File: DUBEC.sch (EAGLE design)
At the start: 46 parts

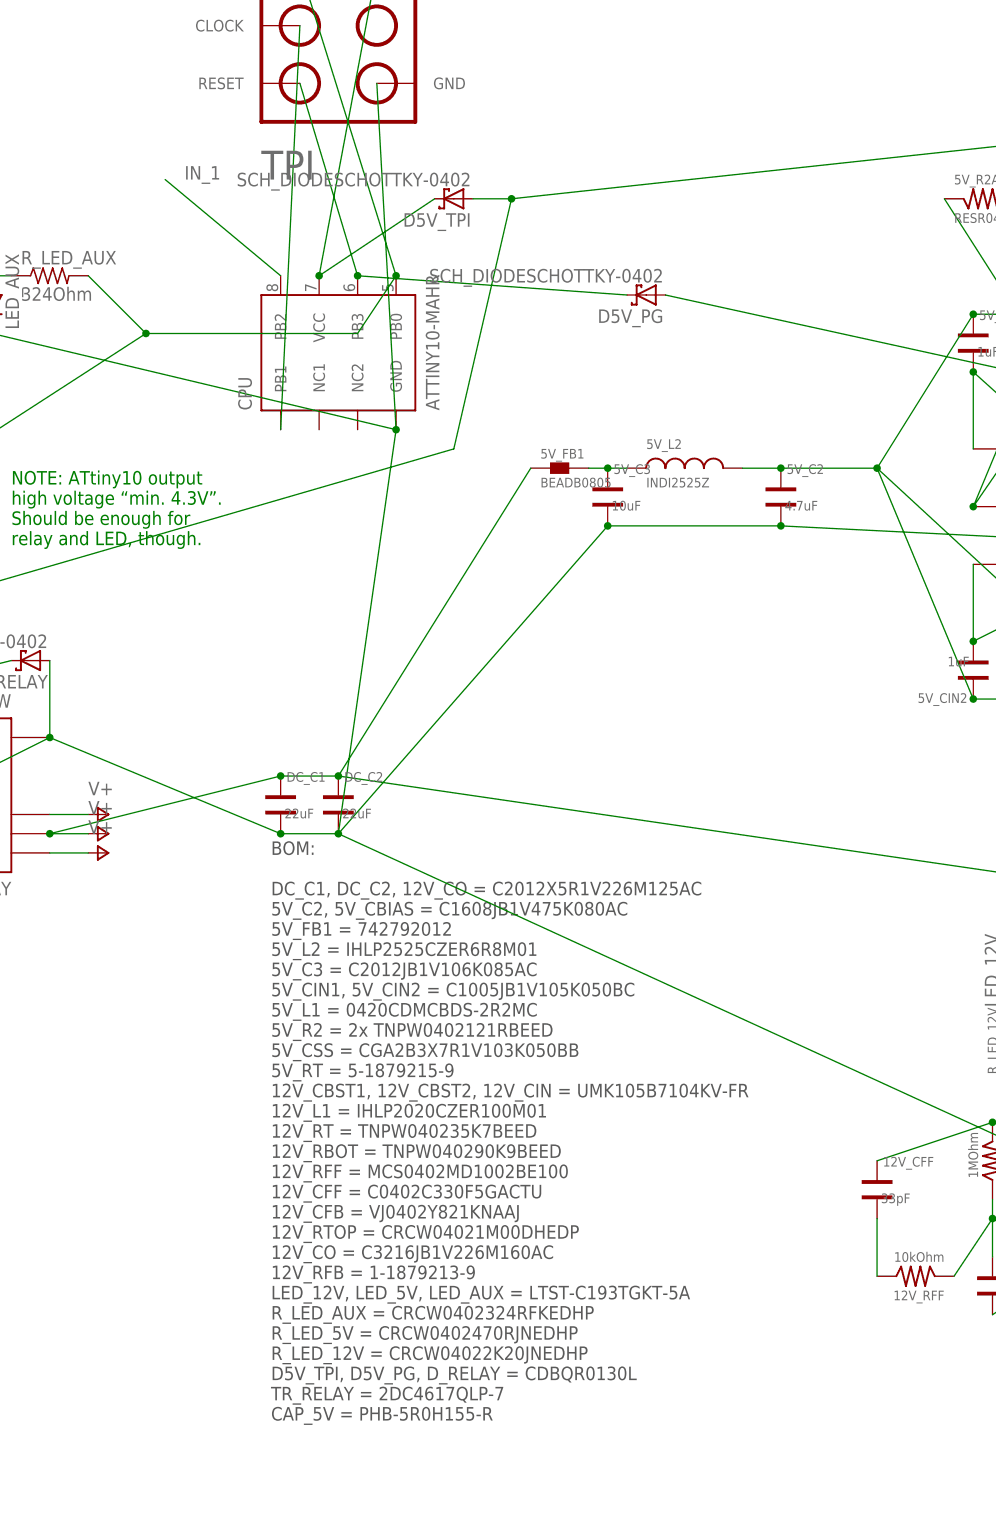
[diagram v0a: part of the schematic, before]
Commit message: Preci-Dip TPI socket
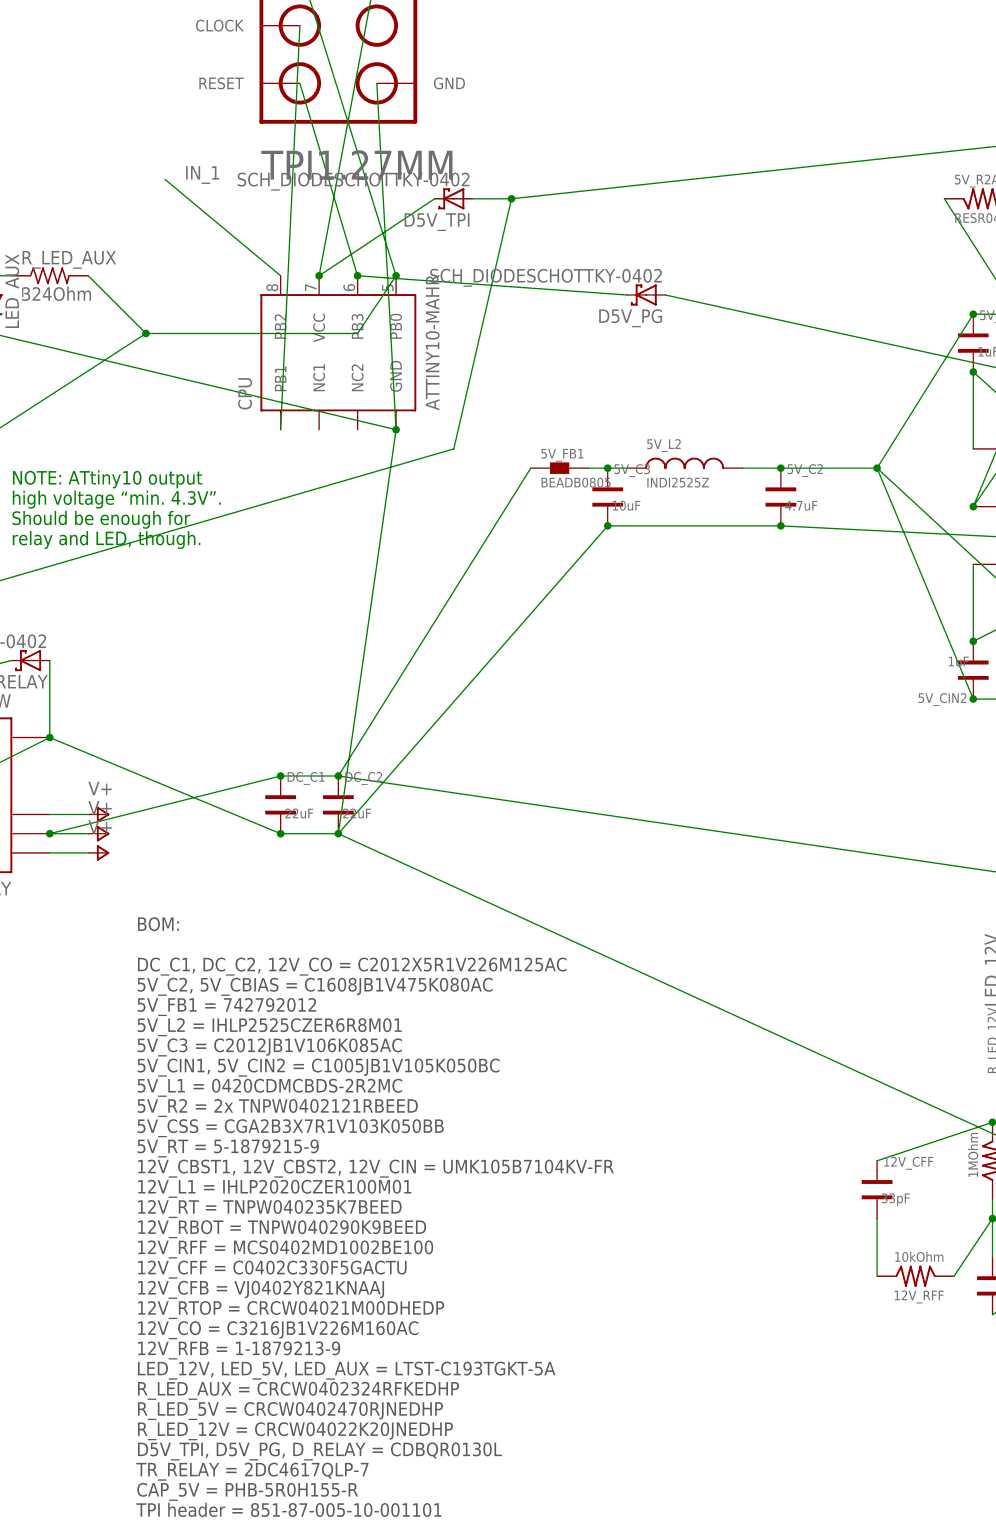
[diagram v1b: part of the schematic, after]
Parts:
- U$1: value TPI -> TPI1.27MM; device dubec:TPI -> dubec:TPI1.27MM
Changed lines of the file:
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@@
 <part name="R_LED_12V" library="jne" deviceset="RES" device="R0402" value="2.2kOhm"/>
 <part name="R_LED_5V" library="jne" deviceset="RES" device="R0402" value="470Ohm"/>
-<part name="U$1" library="dubec" deviceset="TPI" device=""/>
+<part name="U$1" library="dubec" deviceset="TPI" device="1.27MM" value="TPI1.27MM"/>
 <part name="D5V_PG" library="dubec" deviceset="SCH_DIODE" device="SCHOTTKY-0402"/>
 <part name="D5V_TPI" library="dubec" deviceset="SCH_DIODE" device="SCHOTTKY-0402"/>
@@
 <sheet>
 <plain>
-<text x="-49.53" y="-95.25" size="1.778" layer="97">BOM:
+<text x="-67.31" y="-107.95" size="1.778" layer="97">BOM:
 DC_C1, DC_C2, 12V_CO = C2012X5R1V226M125AC
 5V_C2, 5V_CBIAS = C1608JB1V475K080AC
@@
 TR_RELAY = 2DC4617QLP-7
 CAP_5V = PHB-5R0H155-R
+TPI header = 851-87-005-10-001101
 </text>
 <text x="-83.82" y="20.32" size="1.778" layer="91">NOTE: ATtiny10 output

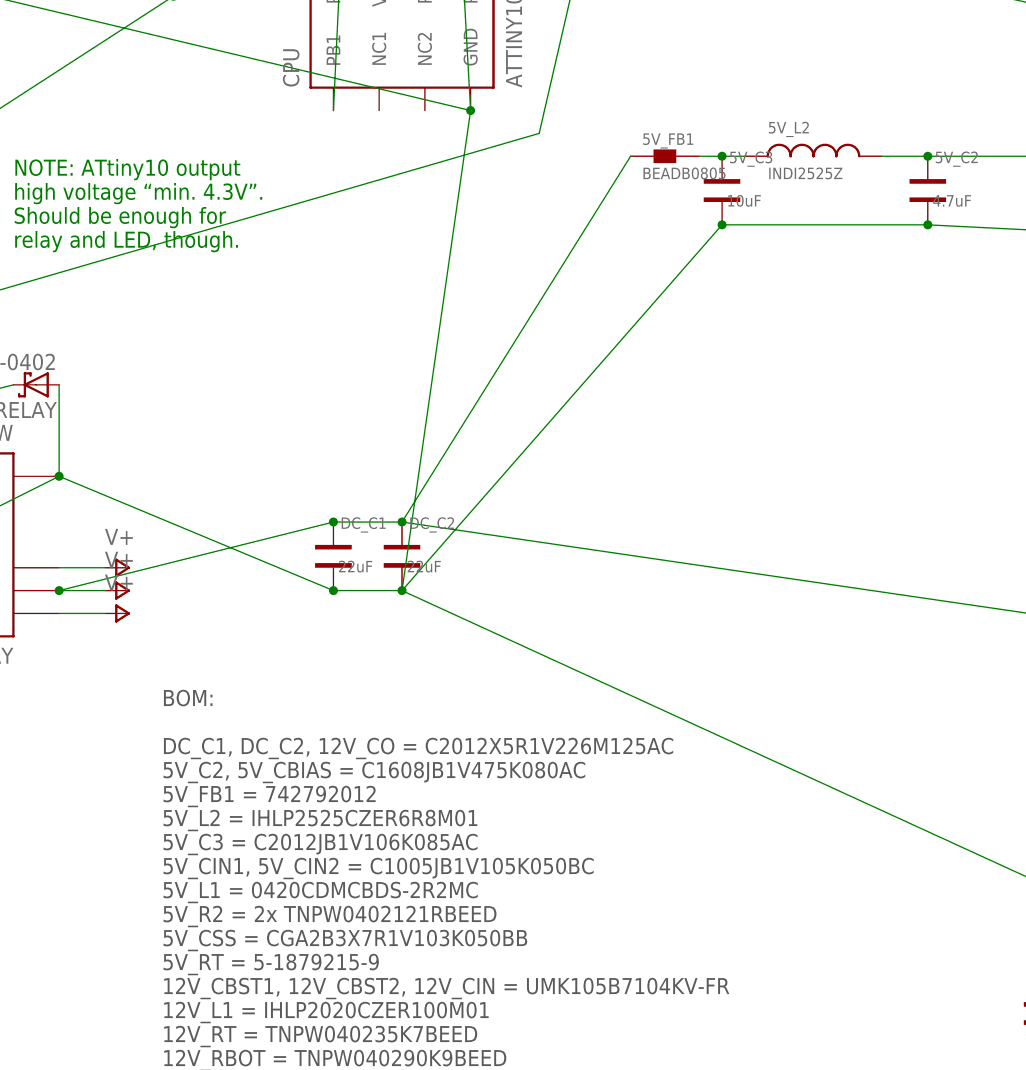
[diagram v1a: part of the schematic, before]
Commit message: Recommended inductor for 5V
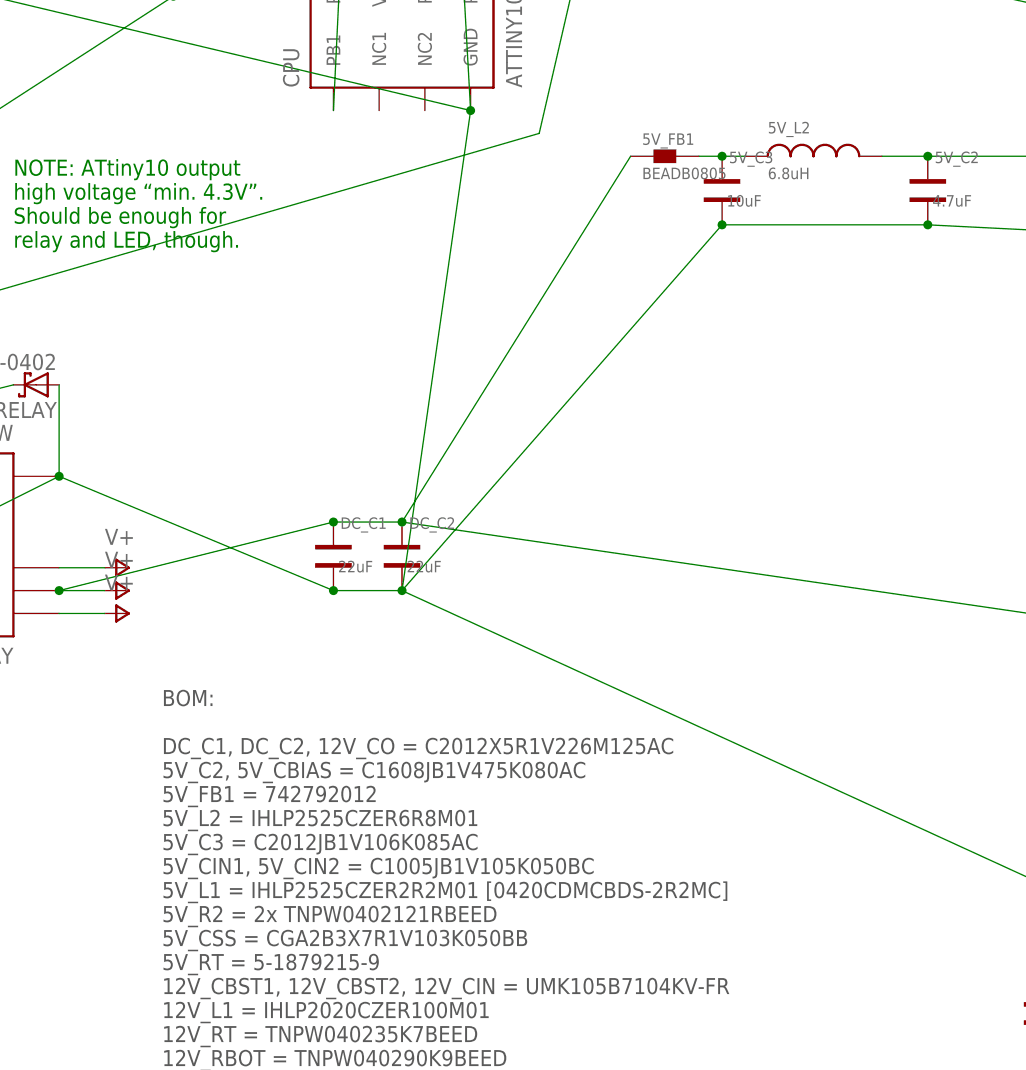
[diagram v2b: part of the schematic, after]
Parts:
- 5V_L1: device jne:INDI0420CDMCB/DS -> dubec:INDI2525Z
- 5V_L2: value INDI2525Z -> 6.8uH
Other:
- note added: "BOM: DC_C1, DC_C2, 12V_CO = C2012X5R1V226M125AC 5V_C2, 5V_CBIAS = C1608JB1V475K080AC 5V_FB1 = 742792012 5V_L2 = IHLP2525CZER6R8M01 5V_C3 = C2012JB1V106K085AC 5V_CIN1, 5V_CIN2 = C1005JB1V105K050BC 5V_L1 = IHLP2525CZER2R2M01 [0420CDMCBDS-2R2MC] 5V_R2 = 2x TNPW0402121RBEED 5V_CSS = CGA2B3X7R1V103K050BB 5V_RT = 5-1879215-9 12V_CBST1, 12V_CBST2, 12V_CIN = UMK105B7104KV-FR 12V_L1 = IHLP2020CZER100M01 1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"
- note removed: "BOM: DC_C1, DC_C2, 12V_CO = C2012X5R1V226M125AC 5V_C2, 5V_CBIAS = C1608JB1V475K080AC 5V_FB1 = 742792012 5V_L2 = IHLP2525CZER6R8M01 5V_C3 = C2012JB1V106K085AC 5V_CIN1, 5V_CIN2 = C1005JB1V105K050BC 5V_L1 = 0420CDMCBDS-2R2MC 5V_R2 = 2x TNPW0402121RBEED 5V_CSS = CGA2B3X7R1V103K050BB 5V_RT = 5-1879215-9 12V_CBST1, 12V_CBST2, 12V_CIN = UMK105B7104KV-FR 12V_L1 = IHLP2020CZER100M01 12V_RT = TNPW040235K7B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"
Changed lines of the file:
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@@
 <part name="DC_C1" library="jne" deviceset="CAP" device="C0805" value="22uF"/>
 <part name="5V_C2" library="jne" deviceset="CAP" device="C0603" value="4.7uF"/>
-<part name="5V_L2" library="jne" deviceset="IND" device="I2525Z" value="INDI2525Z"/>
+<part name="5V_L2" library="jne" deviceset="IND" device="I2525Z" value="6.8uH"/>
 <part name="5V_FB1" library="jne" deviceset="BEAD" device="B0805"/>
 <part name="5V_C3" library="jne" deviceset="CAP" device="C0805" value="10uF"/>
@@
 <part name="12V_CO" library="jne" deviceset="CAP" device="C1206" value="22uF"/>
 <part name="12V_CIN" library="jne" deviceset="CAP" device="C0402" value="0.1uF"/>
-<part name="5V_L1" library="jne" deviceset="IND" device="I0420CDMCB/DS" value="2.2uH"/>
+<part name="5V_L1" library="dubec" deviceset="IND" device="I2525Z" value="2.2uH"/>
 <part name="5V_CBST" library="jne" deviceset="CAP" device="C0402" value="0.1uF"/>
 <part name="5V_CVCC" library="jne" deviceset="CAP" device="C0402" value="1uF"/>
@@
 5V_C3 = C2012JB1V106K085AC
 5V_CIN1, 5V_CIN2 = C1005JB1V105K050BC
-5V_L1 = 0420CDMCBDS-2R2MC
+5V_L1 = IHLP2525CZER2R2M01 [0420CDMCBDS-2R2MC]
 5V_R2 = 2x TNPW0402121RBEED
 5V_CSS = CGA2B3X7R1V103K050BB

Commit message: Flyback diode
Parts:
- added D12V: SCH_DIODESCHOTTKY-0402, dubec:SCH_DIODESCHOTTKY-0402
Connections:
- net GND: now also D12V.A
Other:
- moved on the sheet: 12V_C3, 12V_CBST1, 12V_CBST2, 12V_CFB, 12V_CFF, 12V_CIN, 12V_CO, 12V_RFF, 12V_RT, 5V_C2, 5V_C3, 5V_CIN1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

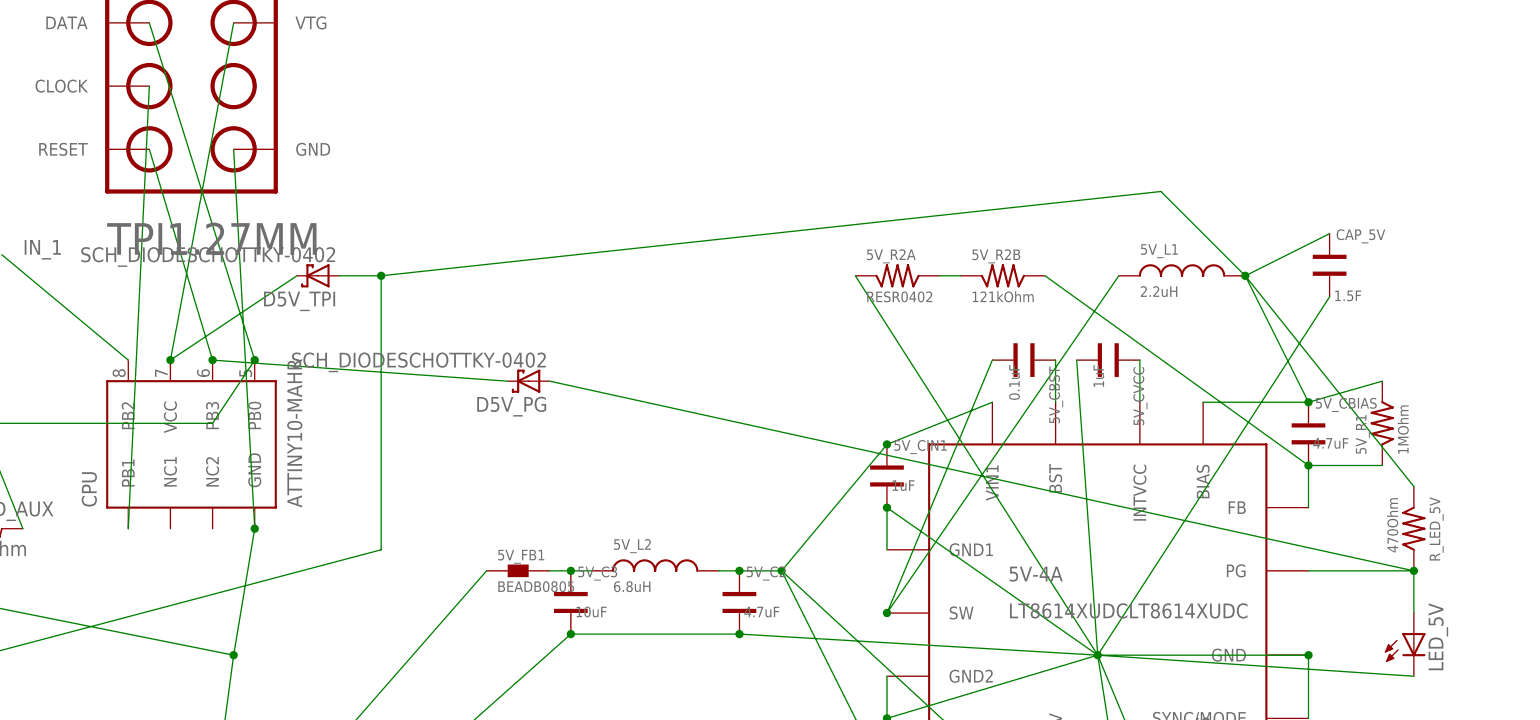
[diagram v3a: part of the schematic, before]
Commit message: Removing PGOOD
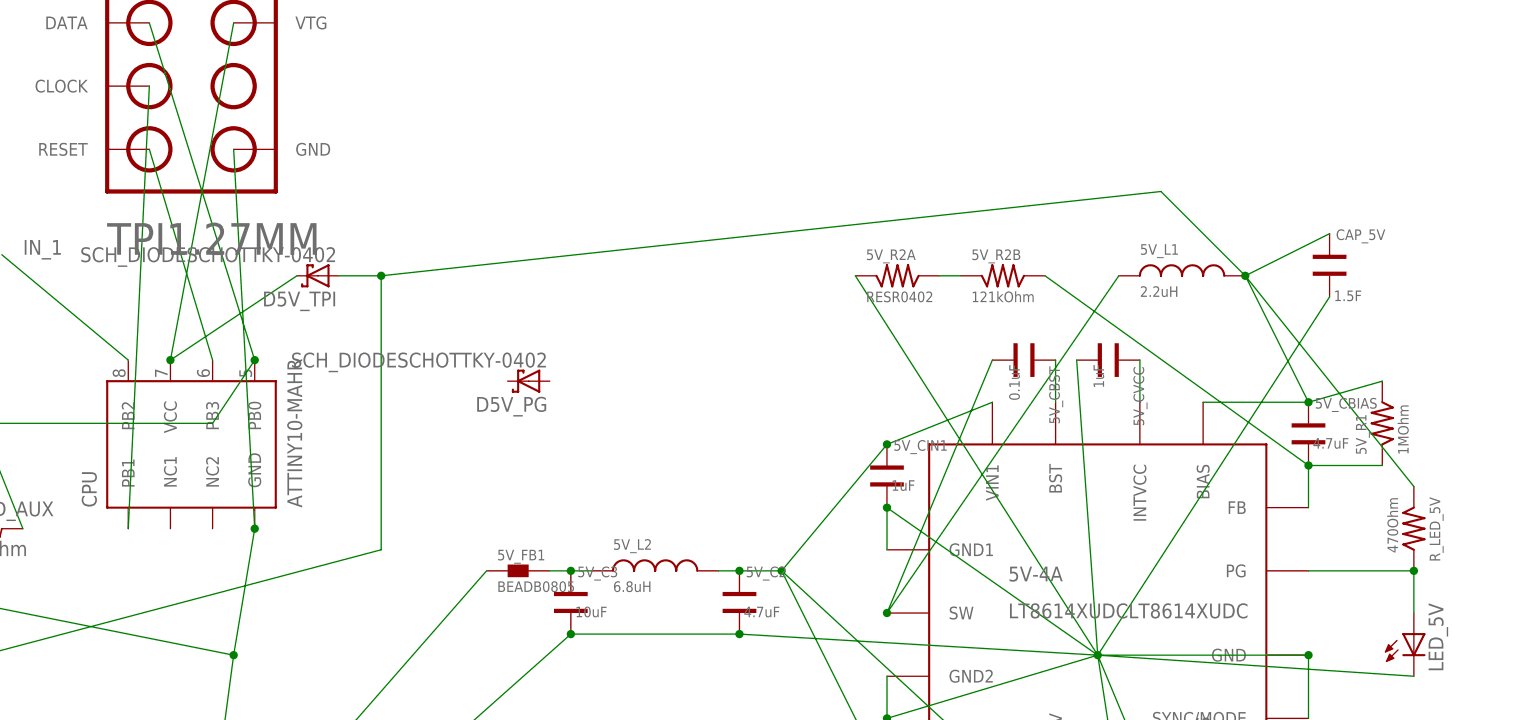
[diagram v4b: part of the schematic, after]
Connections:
- new net PB3: CPU.PB3, U$1.RESET
- net 5V_PG: no longer CPU.PB3, D5V_PG.A, D5V_PG.C, U$1.RESET
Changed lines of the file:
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@@
 <net name="5V_PG" class="0">
-<segment>
-<pinref part="CPU" gate="G$1" pin="PB3"/>
-<pinref part="U$1" gate="G$1" pin="RESET"/>
-<wire x1="-38.1" y1="55.88" x2="-45.72" y2="81.28" width="0.1524" layer="91"/>
-<pinref part="D5V_PG" gate="G$1" pin="C"/>
-<wire x1="-38.1" y1="55.88" x2="-2.54" y2="53.34" width="0.1524" layer="91"/>
-<junction x="-38.1" y="55.88"/>
-</segment>
 <segment>
 <pinref part="5V-4A" gate="G$1" pin="PG"/>
@@
 <junction x="106.68" y="30.48"/>
 <wire x1="106.68" y1="30.48" x2="93.98" y2="30.48" width="0.1524" layer="91"/>
-<pinref part="D5V_PG" gate="G$1" pin="A"/>
-<wire x1="2.54" y1="53.34" x2="106.68" y2="30.48" width="0.1524" layer="91"/>
 </segment>
 </net>
@@
 </segment>
 </net>
+<net name="PB3" class="0">
+<segment>
+<pinref part="U$1" gate="G$1" pin="RESET"/>
+<pinref part="CPU" gate="G$1" pin="PB3"/>
+<wire x1="-45.72" y1="81.28" x2="-38.1" y2="55.88" width="0.1524" layer="91"/>
+</segment>
+</net>
